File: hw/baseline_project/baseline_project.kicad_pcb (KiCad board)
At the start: 2 copper layers, 80 x 143.7 mm, 46 parts, among them IC1 LM4041CILPR, J1 AudioJack, J2 Header_4, SW1 RESET, SW101 UP, SW102 DOWN, SW103 LEFT, SW104 RIGHT, SW105 MODE, U1 TLV5616CP, U101 EK-TM4C123GXL, U102 ESP8266-01/ESP-01, U103 Adafruit ST7735R, U3 LM2937xMP, U4 MCP34119P

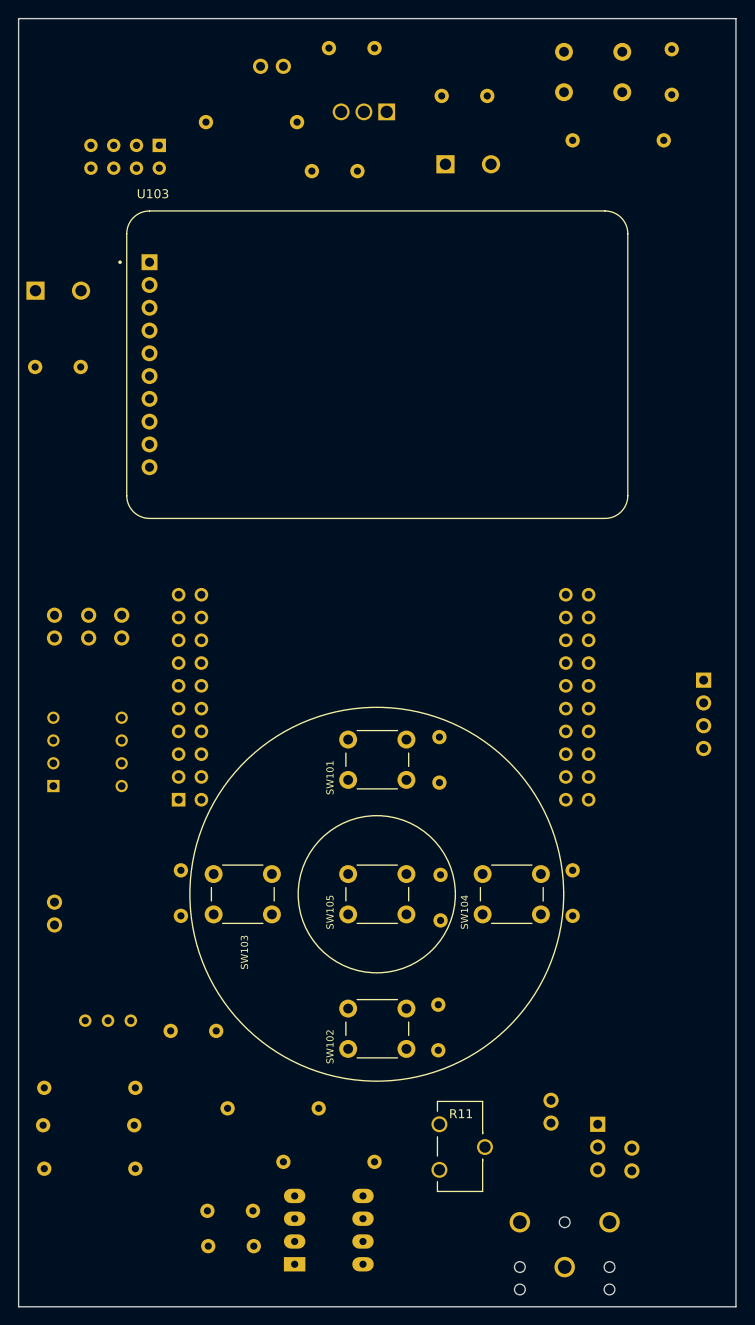
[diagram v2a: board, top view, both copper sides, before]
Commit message: routed ST7735
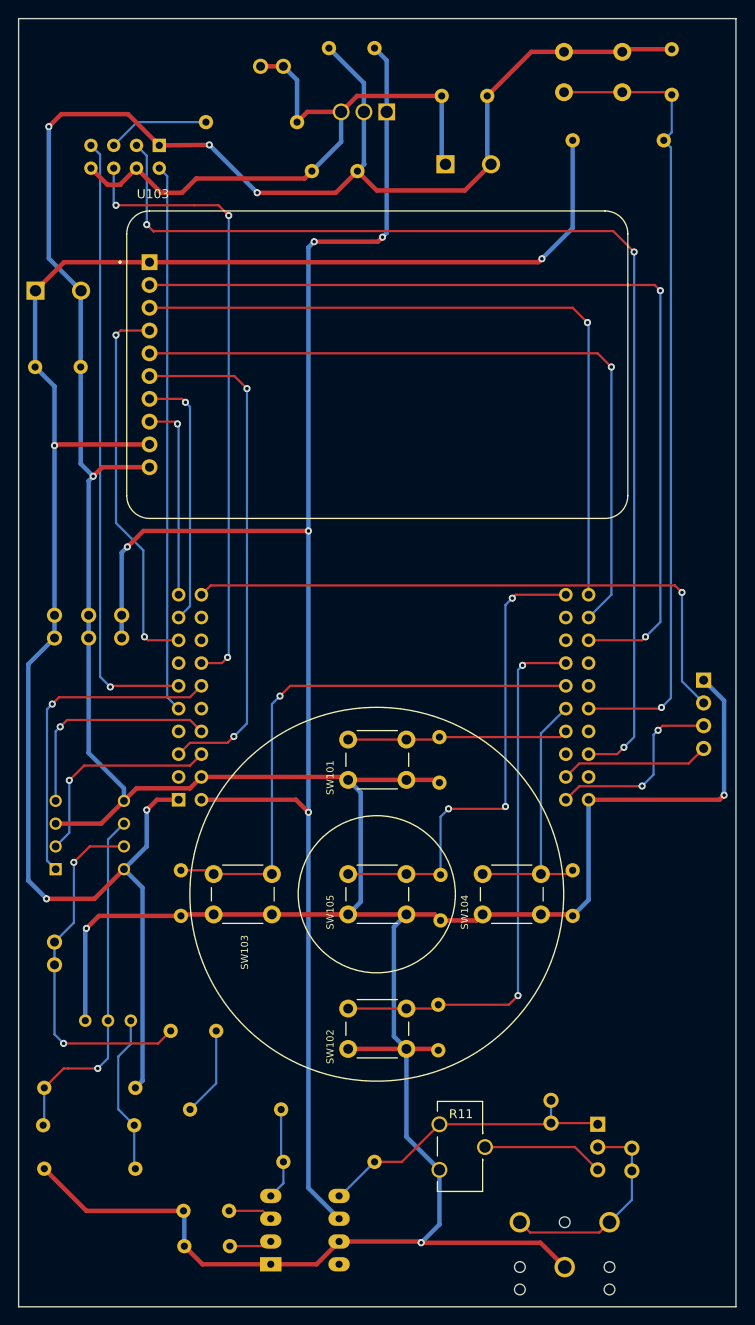
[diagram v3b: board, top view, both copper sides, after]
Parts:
- moved U1 9.27 mm to (31.8, 124.6)
- moved TP2 4.45 mm to (24.0, 140.3)
- moved R1 4.19 mm to (39.1, 159.0)
- moved C3 2.67 mm to (43.6, 174.2)
- moved C1 2.67 mm to (43.5, 170.3)
- moved U4 2.67 mm to (48.1, 176.3)
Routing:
- net GND: track 0.00 -> 475.9 mm, vias 0 -> 7
- net +3V3: track 0.00 -> 201.3 mm, vias 0 -> 4
- net +5V: track 0.00 -> 184.2 mm, vias 0 -> 5
- net /WIFI_IO2: track 0.00 -> 124.9 mm, vias 0 -> 3
- net /TFT_MISO: track 0.00 -> 103.0 mm, vias 0 -> 2
- net /RST: track 0.00 -> 89.8 mm, vias 0 -> 1
- net /TFT_CS: track 0.00 -> 81.1 mm, vias 0 -> 1
- net /TFT_SCK: track 0.00 -> 79.9 mm, vias 0 -> 1
- net /WIFI_3V3: track 0.00 -> 70.8 mm
- net /~{WIFI_RST}: track 0.00 -> 69.8 mm, vias 0 -> 3
- net /WIFI_RXD: track 0.00 -> 69.0 mm, vias 0 -> 1
- net /RED_LED: track 0.00 -> 67.7 mm, vias 0 -> 1
- net /SW_LEFT: track 0.00 -> 62.9 mm, vias 0 -> 1
- net /SW_DOWN: track 0.00 -> 61.5 mm, vias 0 -> 2
- net /WIFI_TXD: track 0.00 -> 61.2 mm
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
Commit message: before changing display
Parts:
- added H1: ~, ECE445L:MountingHole_4_40, F.Cu at (25.0, 176.0)
- added H2: ~, ECE445L:MountingHole_4_40, F.Cu at (95.0, 176.0)
- added H3: ~, ECE445L:MountingHole_4_40, F.Cu at (25.0, 60.0)
- added H4: ~, ECE445L:MountingHole_4_40, F.Cu at (95.0, 60.0)
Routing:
- net GND: track 475.9 -> 477.5 mm
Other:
- board text added: "3V3"
- board text added: "5V"
- board text added: "Amp_Out"
- board text added: "DAC_Amp_Ctrl"
- board text added: "DAC_Out"
- board text added: "GND"
- board text added: "Volume"
- board text added: "Volume_Jmp"
- board text added: "WIFI_3V3"

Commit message: so far so good new display pcb
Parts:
- removed C102: 100nF, ECE445L:C_Axial_200mil
- removed C104: 4.7uF, ECE445L:CP_Radial_Tantal200mil
- removed U103: Adafruit ST7735R, ECE445L:adafruit_st7735r
- added C12: 100nF, ECE445L:C_Axial_200mil, B.Cu at (102.8, 43.2)
- added C13: 4.7uF, ECE445L:CP_Radial_Tantal200mil, B.Cu at (102.7, 50.3)
- added U2: ILI_Display, ECE445L:TFT-320x240, F.Cu at (103.1, 72.8)
- moved C103 87.8 mm to (153.7, 36.4)
- moved C11 87.8 mm to (178.9, 28.7)
- moved C5 87.8 mm to (138.8, 37.2)
- moved R12 87.8 mm to (178.1, 33.8)
- moved TP7 87.8 mm to (133.1, 25.5)
- moved U102 87.8 mm to (118.0, 26.0)
- moved C4 87.8 mm to (145.8, 23.5)
- moved H3 87.8 mm to (111.1, 42.9)
- moved H4 87.8 mm to (181.1, 42.9)
- moved R101 87.8 mm to (137.2, 31.8)
- moved SW1 87.8 mm to (173.4, 23.9)
- moved U3 87.8 mm to (147.2, 30.6)
- moved C101 87.8 mm to (153.3, 28.8)
- moved C10 86.3 mm to (153.0, 125.8)
- moved C9 86.3 mm to (167.8, 125.2)
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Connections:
- U101 pad J1_4: unconnected-(U101-PB1-PadJ1_4) -> /Touch_CS
- U101 pad J1_7: unconnected-(U101-PB4-PadJ1_7) -> /SS2_SCLK
- U101 pad J2_2: unconnected-(U101-PB2-PadJ2_2) -> /Touch_IRQ
- U101 pad J2_6: unconnected-(U101-PB7-PadJ2_6) -> /SS2_TX
- U101 pad J2_7: unconnected-(U101-PB6-PadJ2_7) -> /SS2_RX
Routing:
- net /SDC_CS: track 57.8 -> 0.00 mm, vias 2 -> 0
- net GND: track 477.5 -> 507.6 mm
- net /TFT_RST: track 22.3 -> 50.4 mm
- net +3V3: track 201.3 -> 227.3 mm, vias 4 -> 5
- net /TFT_D/C: track 28.9 -> 52.1 mm
- net /TFT_CS: track 81.1 -> 104.0 mm
- net /WIFI_IO2: track 124.9 -> 135.0 mm
- net /RST: track 89.4 -> 99.5 mm
- net /WIFI_RXD: track 69.0 -> 79.1 mm
- net /~{WIFI_RST}: track 69.8 -> 79.9 mm
- net /WIFI_TXD: track 61.2 -> 71.3 mm
- net +5V: track 184.2 -> 194.3 mm
- net /TFT_SCK: track 79.9 -> 88.5 mm
- net /TFT_MISO: track 103.0 -> 94.8 mm
- net /TFT_MOSI: track 42.9 -> 49.8 mm
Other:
- board size 80 x 143.7 mm -> 100 x 153.7 mm

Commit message: pcb done
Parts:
- moved C13 5.39 mm to (105.8, 45.8)
- moved C12 4.98 mm to (105.7, 39.1)
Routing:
- net /SS2_TX: track 0.00 -> 138.4 mm, vias 0 -> 2
- net /SS2_SCLK: track 0.00 -> 129.8 mm, vias 0 -> 1
- net /SS2_RX: track 0.00 -> 127.9 mm, vias 0 -> 2
- net /SDC_CS: track 0.00 -> 99.1 mm, vias 0 -> 2
- net /Touch_IRQ: track 0.00 -> 92.1 mm, vias 0 -> 3
- net /Touch_CS: track 0.00 -> 49.4 mm, vias 0 -> 1
- net GND: track 507.6 -> 510.4 mm
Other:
- board size 100 x 153.7 mm -> 93.5 x 153.7 mm
- board text added: "ECE445L Final - TPod Prithvi Senthilkumar Joon Song Siddhant Pandit Wyatt Cole"
